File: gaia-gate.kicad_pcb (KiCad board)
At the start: 2 copper layers, 96.5 x 74.9 mm, 15 parts, among them J1 Conn_01x02_Male, J2 Conn_01x06_Male, J3 Conn_01x03, J4 Conn_01x06_Male, J5 Conn_01x02_Male, J6 Conn_01x01_Male, J7 Conn_01x01_Male, U1 Vcc_one_supply, U2 ATmega328P-PU, Y1 Crystal

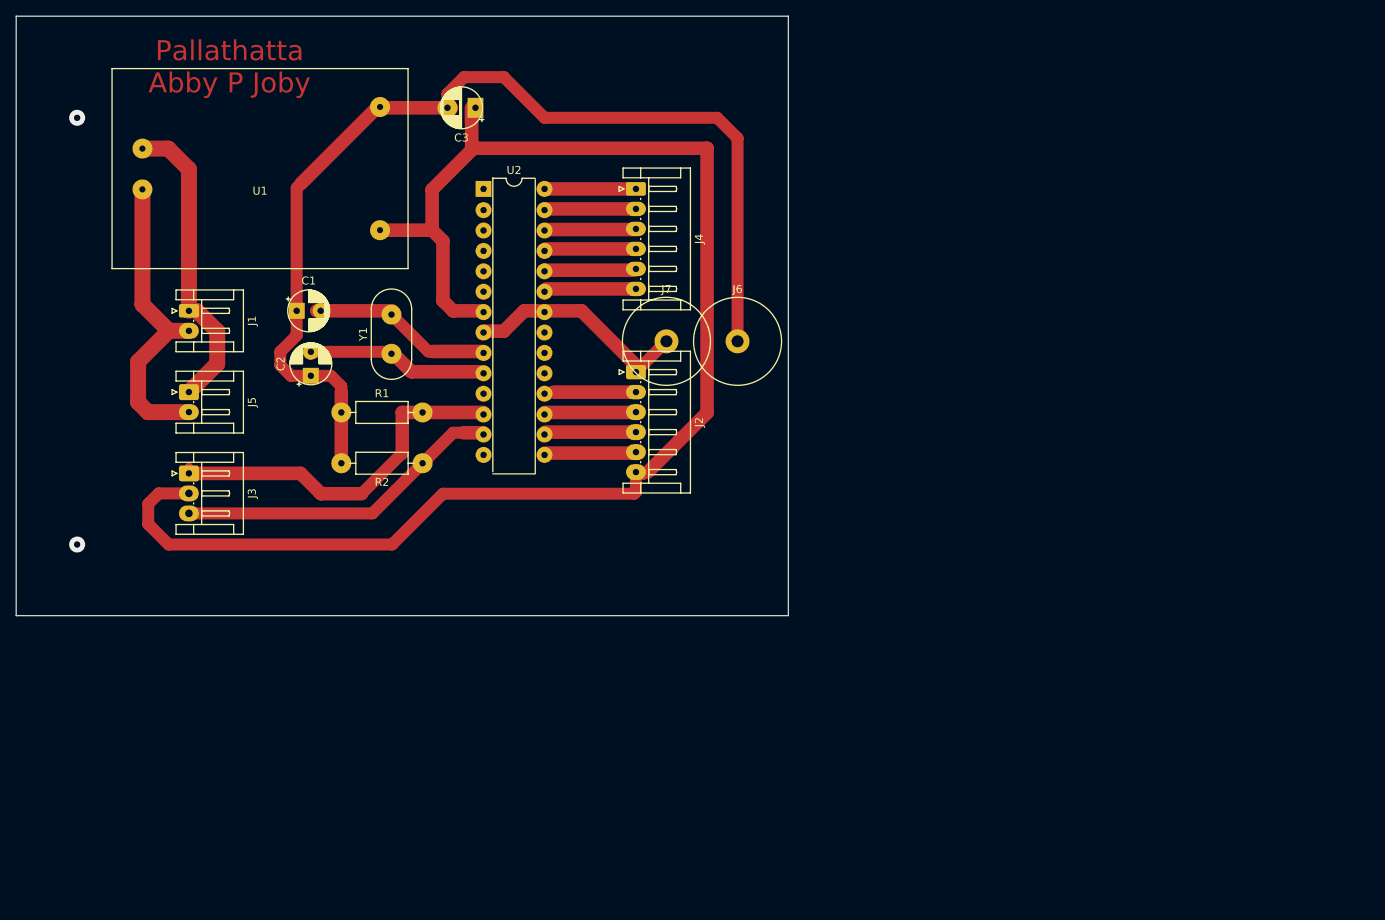
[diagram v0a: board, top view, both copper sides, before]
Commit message: v2 withcontrol board circuit
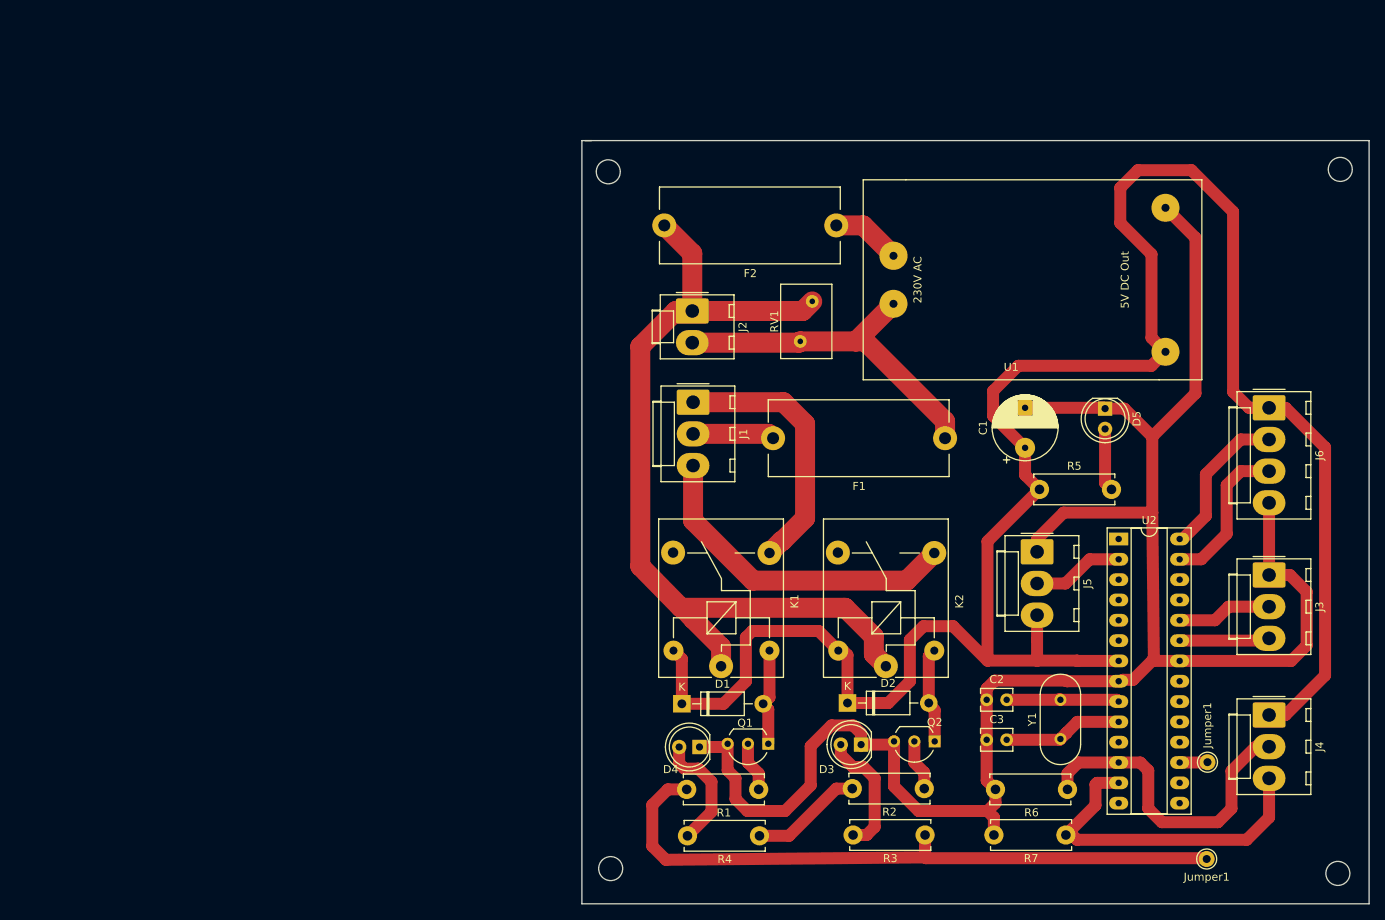
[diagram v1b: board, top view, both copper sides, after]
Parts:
- removed J7: Conn_01x01_Male, Connector:Banana_Jack_1Pin
- added  : MountingHole_3mm, MountingHole:MountingHole_3mm, F.Cu at (95.6, 38.5)
- added  : MountingHole_3mm, MountingHole:MountingHole_3mm, F.Cu at (95.9, 125.6)
- added  : MountingHole_3mm, MountingHole:MountingHole_3mm, F.Cu at (186.8, 126.2)
- added  : MountingHole_3mm, MountingHole:MountingHole_3mm, F.Cu at (187.1, 38.2)
- added D1: 1N4007, Diode_THT:D_DO-41_SOD81_P10.16mm_Horizontal, F.Cu at (104.8, 105.0)
- added D2: 1N4007, Diode_THT:D_DO-41_SOD81_P10.16mm_Horizontal, F.Cu at (125.5, 104.9)
- added D3: GREEN, LED_THT:LED_D5.0mm, F.Cu at (127.2, 110.1)
- added D4: GREEN, LED_THT:LED_D5.0mm, F.Cu at (107.0, 110.4)
- added D5: GREEN, LED_THT:LED_D5.0mm, F.Cu at (157.7, 68.1)
- added F1: Fuse, gaia-gate:Fuse, F.Cu at (138.2, 71.8)
- added F2: Fuse, gaia-gate:Fuse, F.Cu at (124.6, 45.2)
- added Jumper1: Pin_D1.0mm_L10.0mm, Connector_Pin:Pin_D1.0mm_L10.0mm, F.Cu at (170.4, 124.4)
- added Jumper1: Pin_D1.0mm_L10.0mm, Connector_Pin:Pin_D1.0mm_L10.0mm, F.Cu at (170.5, 112.3)
- added K1: SANYOU_SRD_Form_C, Relay_THT:Relay_SPDT_SANYOU_SRD_Series_Form_C, F.Cu at (109.7, 100.3)
- added K2: SANYOU_SRD_Form_C, Relay_THT:Relay_SPDT_SANYOU_SRD_Series_Form_C, F.Cu at (130.3, 100.3)
- added Q1: BC547, Package_TO_SOT_THT:TO-92_Inline_Wide, F.Cu at (115.6, 110.0)
- added Q2: BC547, Package_TO_SOT_THT:TO-92_Inline_Wide, F.Cu at (136.4, 109.7)
- added R3: 330Ω, gaia-gate:resistor, F.Cu at (137.2, 121.4)
- added R4: 330Ω, gaia-gate:resistor, F.Cu at (116.5, 121.5)
- added R5: 330Ω, gaia-gate:resistor, F.Cu at (147.5, 78.2)
- added R6: 100K, gaia-gate:resistor, F.Cu at (142.0, 115.7)
- added R7: 100K, gaia-gate:resistor, F.Cu at (154.8, 121.4)
- added RV1: Varistor, Varistor:RV_Disc_D9mm_W6.1mm_P5mm, F.Cu at (121.1, 54.7)
- C1: value C -> CP; footprint Capacitor_THT:CP_Radial_D5.0mm_P2.00mm -> Capacitor_THT:CP_Radial_D8.0mm_P5.00mm
- C2: footprint Capacitor_THT:CP_Radial_D5.0mm_P2.00mm -> Capacitor_THT:C_Disc_D3.8mm_W2.6mm_P2.50mm
- C3: value CP -> C; footprint Capacitor_THT:CP_Radial_D5.0mm_P2.50mm -> Capacitor_THT:C_Disc_D3.8mm_W2.6mm_P2.50mm
- J1: value Conn_01x02_Male -> motor; footprint Connector_JST:JST_EH_S2B-EH_1x02_P2.50mm_Horizontal -> Connector_Molex:Molex_KK-396_A-41791-0003_1x03_P3.96mm_Vertical
- J2: value Conn_01x06_Male -> 230V_IN; footprint Connector_JST:JST_EH_S6B-EH_1x06_P2.50mm_Horizontal -> Connector_Molex:Molex_KK-396_A-41791-0002_1x02_P3.96mm_Vertical
- J3: value Conn_01x03 -> Control_Signal_IN; footprint Connector_JST:JST_EH_S3B-EH_1x03_P2.50mm_Horizontal -> Connector_Molex:Molex_KK-396_A-41791-0003_1x03_P3.96mm_Vertical
- J4: value Conn_01x06_Male -> Conn_01x03; footprint Connector_JST:JST_EH_S6B-EH_1x06_P2.50mm_Horizontal -> Connector_Molex:Molex_KK-396_A-41791-0003_1x03_P3.96mm_Vertical
- J5: value Conn_01x02_Male -> Extras; footprint Connector_JST:JST_EH_S2B-EH_1x02_P2.50mm_Horizontal -> Connector_Molex:Molex_KK-396_A-41791-0003_1x03_P3.96mm_Vertical
- J6: value Conn_01x01_Male -> extra_analog; footprint Connector:Banana_Jack_1Pin -> Connector_Molex:Molex_KK-396_A-41791-0004_1x04_P3.96mm_Vertical
- R1, R2: value 100K -> 1K; footprint Resistor_THT:R_Axial_DIN0207_L6.3mm_D2.5mm_P10.16mm_Horizontal -> gaia-gate:resistor
- U1: footprint gaia-gate:VREG_230Vac_to_5Vdc -> gaia-gate:230_5V_supply_HiLink
- U2: footprint Package_DIP:DIP-28_W7.62mm -> Package_DIP:DIP-28_W7.62mm_Socket_LongPads
- moved J3 135.6 mm to (178.2, 88.9)
- moved J5 107.9 mm to (149.2, 86.0)
- moved J4 102.9 mm to (178.2, 106.4)
- moved C3 101.9 mm to (142.9, 109.5), turned to 0 degrees
- moved U1 97.2 mm to (148.2, 52.0)
- moved Y1 96.5 mm to (152.1, 109.4)
- moved C2 93.9 mm to (142.9, 104.5), turned to 0 degrees
- moved C1 92.2 mm to (147.7, 73.0), turned to 90 degrees
- moved U2 90.7 mm to (159.4, 84.4)
- moved R2 76.4 mm to (137.1, 115.6)
- moved R1 71.8 mm to (116.4, 115.7), turned to 180 degrees
- moved J6 67.0 mm to (178.2, 68.0), turned to 270 degrees
- moved J1 64.0 mm to (106.2, 67.3)
- moved J2 10.4 mm to (106.1, 55.9)
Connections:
- C1 pad 1: GND -> +5V
- C1 pad 2: Net-(C1-Pad2) -> GND
- C3 pad 1: +5V -> GND
- C3 pad 2: GND -> Net-(C3-Pad2)
- J1 pad 2: Net-(J1-Pad2) -> Net-(F1-Pad2)
- J2 pad 1: GND -> AC
- J2 pad 2: Net-(J2-Pad2) -> NEUT
- J3 pad 1: Net-(J3-Pad1) -> GND
- J3 pad 2: +5V -> Net-(J3-Pad2)
- J4 pad 1: Net-(J4-Pad1) -> +5V
- J5 pad 1: Net-(J1-Pad1) -> GND
- J5 pad 2: Net-(J1-Pad2) -> Net-(J5-Pad2)
- J6 pad 1: GND -> +5V
- R1 pad 1: GND -> Net-(Q1-Pad2)
- R1 pad 2: Net-(J3-Pad1) -> Relay1_IN
- R2 pad 1: Net-(J3-Pad3) -> Net-(Q2-Pad2)
- R2 pad 2: GND -> Relay2_IN
- U1 pad 1: Net-(J1-Pad1) -> Net-(F2-Pad1)
- U1 pad 2: Net-(J1-Pad2) -> NEUT
- U2 pad 10: Net-(C2-Pad2) -> Net-(C3-Pad2)
- U2 pad 12: Net-(J3-Pad1) -> Net-(J4-Pad2)
- U2 pad 13: Net-(J3-Pad3) -> Net-(J4-Pad3)
- U2 pad 15: Net-(J2-Pad5) -> Net-(U2-Pad15)
- U2 pad 16: Net-(J2-Pad4) -> Net-(U2-Pad16)
- U2 pad 17: Net-(J2-Pad3) -> Relay1_IN
- U2 pad 18: Net-(J2-Pad2) -> Net-(U2-Pad18)
- U2 pad 2: Net-(U2-Pad2) -> Net-(J5-Pad2)
- U2 pad 23: Net-(J4-Pad6) -> Net-(J3-Pad3)
- U2 pad 24: Net-(J4-Pad5) -> Net-(J3-Pad2)
- U2 pad 25: Net-(J4-Pad4) -> Net-(U2-Pad25)
- U2 pad 26: Net-(J4-Pad3) -> Net-(U2-Pad26)
- U2 pad 27: Net-(J4-Pad2) -> Net-(J6-Pad3)
- U2 pad 28: Net-(J4-Pad1) -> Net-(J6-Pad2)
- U2 pad 9: Net-(C1-Pad2) -> Net-(C2-Pad2)
- Y1 pad 1: Net-(C2-Pad2) -> Net-(C3-Pad2)
- Y1 pad 2: Net-(C1-Pad2) -> Net-(C2-Pad2)
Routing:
- net AC: track 0.00 -> 109.9 mm
- net Relay1_IN: track 0.00 -> 86.6 mm
- net +5V: track 189.4 -> 267.7 mm
- net GND: track 161.7 -> 237.9 mm
- net Net-(J3-Pad1): track 45.9 -> 0.00 mm
- net NEUT: track 0.00 -> 44.6 mm
- net Net-(J1-Pad3): track 0.00 -> 41.6 mm
- net Net-(J1-Pad2): track 39.0 -> 0.00 mm
- net Net-(C1-Pad2): track 33.5 -> 0.00 mm
- net Net-(J4-Pad3): track 11.5 -> 42.5 mm
- net Net-(J3-Pad3): track 42.3 -> 11.3 mm
- net Net-(J4-Pad2): track 11.4 -> 40.3 mm
- net Net-(J6-Pad2): track 0.00 -> 19.4 mm
- net Net-(J6-Pad3): track 0.00 -> 19.3 mm
- net Net-(D3-Pad2): track 0.00 -> 15.9 mm
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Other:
- board size 96.5 x 74.9 mm -> 98.4 x 95.4 mm
- board text removed: "Pallathatta Abby P Joby"
